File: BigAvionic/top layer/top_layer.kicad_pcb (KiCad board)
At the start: 4 copper layers, 68 x 68 mm, 23 parts, among them J1 Conn_01x08, J2 Conn_Coaxial, J3 Conn_01x04, U1 NEO-M9N-00B, U2 MMC5983MA

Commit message: save
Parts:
- H1, H2, H3, H4: footprint MountingHole:MountingHole_3.2mm_M3 -> MountingHole:MountingHole_3.2mm_M3_DIN965_Pad
- renumbered TP1 to GPS_BOOT
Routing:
- net GND: track 127.3 -> 132.4 mm, vias 15 -> 16

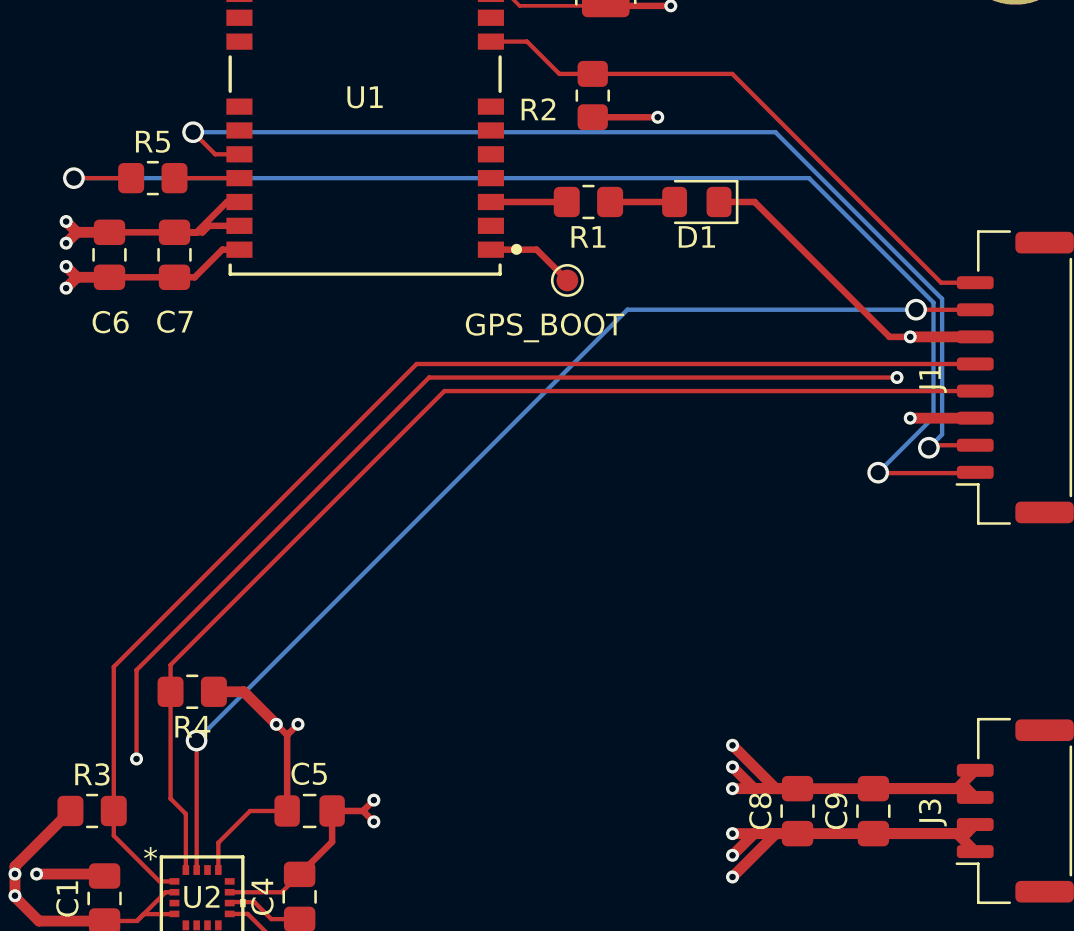
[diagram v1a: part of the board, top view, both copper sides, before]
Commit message: adjust top layer wiring
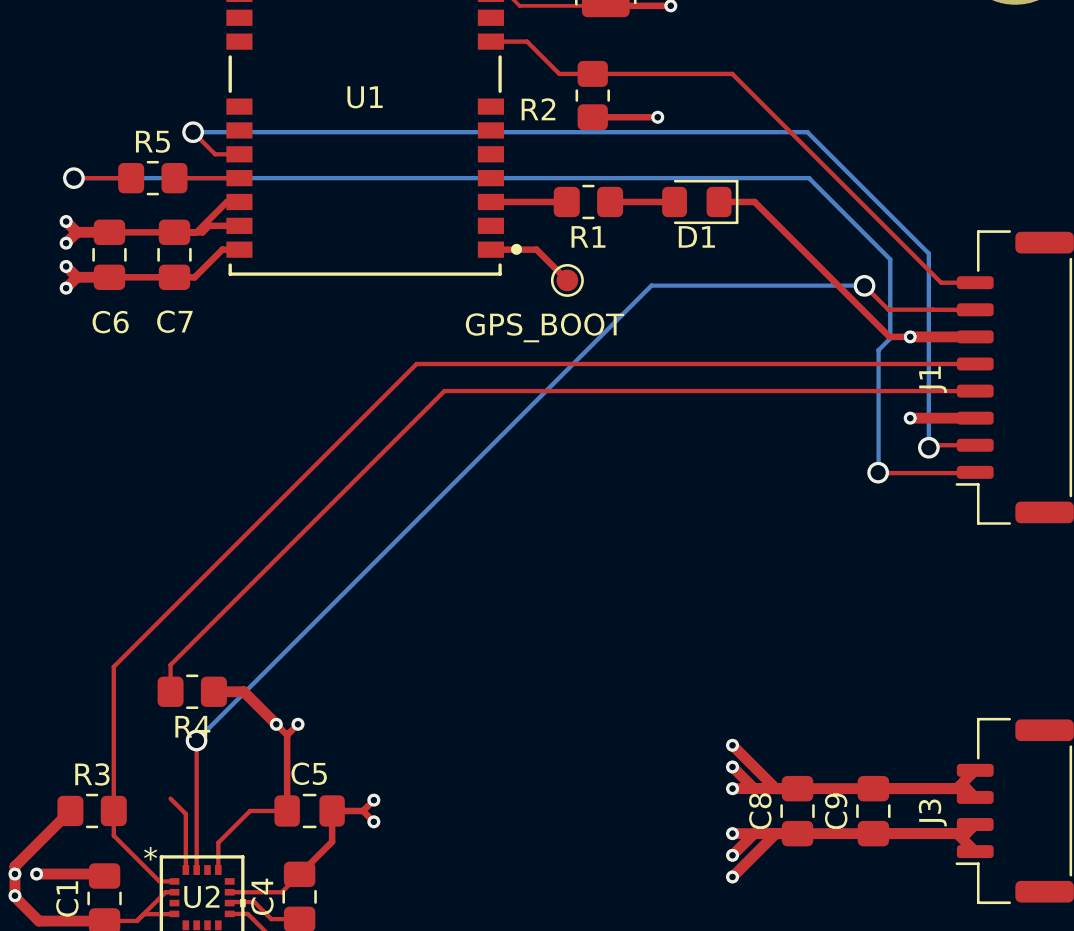
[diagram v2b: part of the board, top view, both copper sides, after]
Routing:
- net GND: track 132.4 -> 87.6 mm, vias 16 -> 14
- net I2C1_SDA: track 52.1 -> 47.2 mm
- net UART6_TX: track 58.0 -> 56.4 mm
- net INT_Magn: track 50.1 -> 51.1 mm
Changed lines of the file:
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@@
-	)
-	(segment
-		(start 135.65 97.3)
-		(end 157.24 97.3)
-		(width 0.2)
-		(layer "F.Cu")
-		(net 1)
 	)
 	(segment
@@
 	)
 	(segment
-		(start 122.15 110.8)
-		(end 135.65 97.3)
-		(width 0.2)
-		(layer "F.Cu")
-		(net 1)
-	)
-	(segment
 		(start 119.402 92.675)
 		(end 118.902 92.175)
@@
 		(end 124.897202 77.399999)
 		(width 0.3)
-		(layer "F.Cu")
-		(net 1)
-	)
-	(segment
-		(start 122.15 114.9)
-		(end 122.15 110.8)
-		(width 0.2)
 		(layer "F.Cu")
 		(net 1)
@@
 	)
 	(via
-		(at 122.15 114.9)
-		(size 0.6)
-		(drill 0.3)
-		(layers "F.Cu" "B.Cu")
-		(free yes)
-		(net 1)
-	)
-	(via
 		(at 118.902 93.175)
 		(size 0.6)
@@
 	)
 	(via
-		(at 157.24 97.3)
-		(size 0.6)
-		(drill 0.3)
-		(layers "F.Cu" "B.Cu")
-		(free yes)
-		(net 1)
-	)
-	(via
 		(at 146.802 80.15)
 		(size 0.6)
@@
 	)
 	(segment
-		(start 123.72 116.73)
-		(end 123.72 111.8)
-		(width 0.2)
-		(layer "F.Cu")
-		(net 6)
-	)
-	(segment
 		(start 156.39 101.71)
 		(end 160.815 101.71)
@@
 	)
 	(segment
+		(start 156.39 101.67)
+		(end 156.39 96.035057)
+		(width 0.2)
+		(layer "B.Cu")
+		(net 7)
+	)
+	(segment
 		(start 156.37 101.69)
-		(end 158.92 99.14)
-		(width 0.2)
-		(layer "B.Cu")
-		(net 7)
-	)
-	(segment
-		(start 158.92 93.837214)
-		(end 153.182786 88.1)
-		(width 0.2)
-		(layer "B.Cu")
-		(net 7)
-	)
-	(segment
-		(start 158.92 99.14)
-		(end 158.92 93.837214)
+		(end 156.39 101.67)
 		(width 0.2)
 		(layer "B.Cu")
@@
 	)
 	(segment
+		(start 156.93 95.495057)
+		(end 156.93 91.847214)
+		(width 0.2)
+		(layer "B.Cu")
+		(net 7)
+	)
+	(segment
+		(start 156.93 91.847214)
+		(end 153.182786 88.1)
+		(width 0.2)
+		(layer "B.Cu")
+		(net 7)
+	)
+	(segment
+		(start 156.39 96.035057)
+		(end 156.93 95.495057)
+		(width 0.2)
+		(layer "B.Cu")
+		(net 7)
+	)
+	(segment
 		(start 135.075 96.675)
 		(end 160.85 96.675)
@@
 	)
 	(segment
-		(start 158.12 94.17)
-		(end 158.9 94.17)
-		(width 0.2)
-		(layer "F.Cu")
-		(net 9)
-	)
-	(segment
 		(start 124.925 120.025001)
 		(end 124.925 114.055)
@@
 	)
 	(segment
+		(start 155.741041 93.068959)
+		(end 156.842082 94.17)
+		(width 0.2)
+		(layer "F.Cu")
+		(net 9)
+	)
+	(segment
+		(start 158.9 94.17)
+		(end 158.905 94.175)
+		(width 0.2)
+		(layer "F.Cu")
+		(net 9)
+	)
+	(segment
 		(start 124.925 114.055)
 		(end 124.92 114.05)
@@
 	)
 	(segment
-		(start 158.9 94.17)
-		(end 158.905 94.175)
+		(start 156.842082 94.17)
+		(end 158.9 94.17)
 		(width 0.2)
 		(layer "F.Cu")
@@
 	)
 	(via
-		(at 158.12 94.17)
+		(at 155.741041 93.068959)
 		(size 1)
 		(drill 0.7)
@@
 	)
 	(segment
-		(start 144.8 94.17)
-		(end 158.12 94.17)
+		(start 155.732082 93.06)
+		(end 145.91 93.06)
 		(width 0.2)
 		(layer "B.Cu")
@@
 	)
 	(segment
-		(start 124.92 114.05)
-		(end 144.8 94.17)
+		(start 145.91 93.06)
+		(end 124.92 114.05)
+		(width 0.2)
+		(layer "B.Cu")
+		(net 9)
+	)
+	(segment
+		(start 155.741041 93.068959)
+		(end 155.732082 93.06)
 		(width 0.2)
 		(layer "B.Cu")
@@
 	)
 	(segment
-		(start 159.321 93.671114)
-		(end 159.321 99.929)
+		(start 153.11 85.98)
+		(end 158.71 91.58)
 		(width 0.2)
 		(layer "B.Cu")
@@
 	)
 	(segment
-		(start 159.321 99.929)
+		(start 124.76 85.98)
+		(end 153.11 85.98)
+		(width 0.2)
+		(layer "B.Cu")
+		(net 10)
+	)
+	(segment
+		(start 158.71 91.58)
 		(end 158.71 100.54)
 		(width 0.2)
 		(layer "B.Cu")
-		(net 10)
-	)
-	(segment
-		(start 124.76 85.98)
-		(end 151.629886 85.98)
-		(width 0.2)
-		(layer "B.Cu")
-		(net 10)
-	)
-	(segment
-		(start 151.629886 85.98)
-		(end 159.321 93.671114)
-		(width 0.2)
-		(layer "B.Cu")
